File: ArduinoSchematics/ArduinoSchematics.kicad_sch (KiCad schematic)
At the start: 15 parts

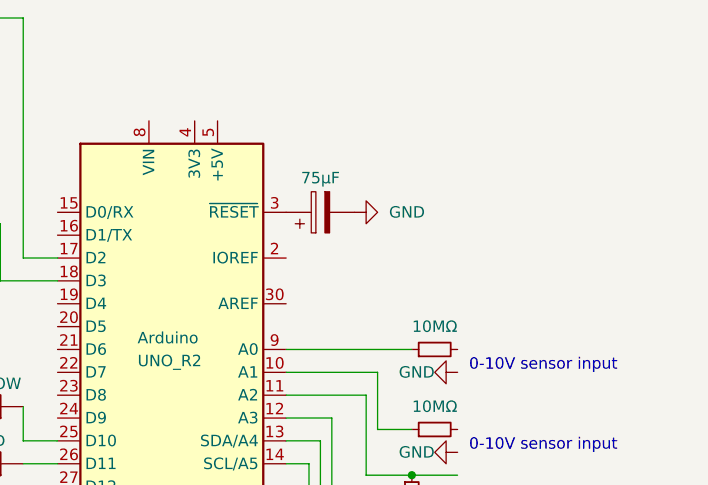
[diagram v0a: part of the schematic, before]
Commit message: Added switch to schematics
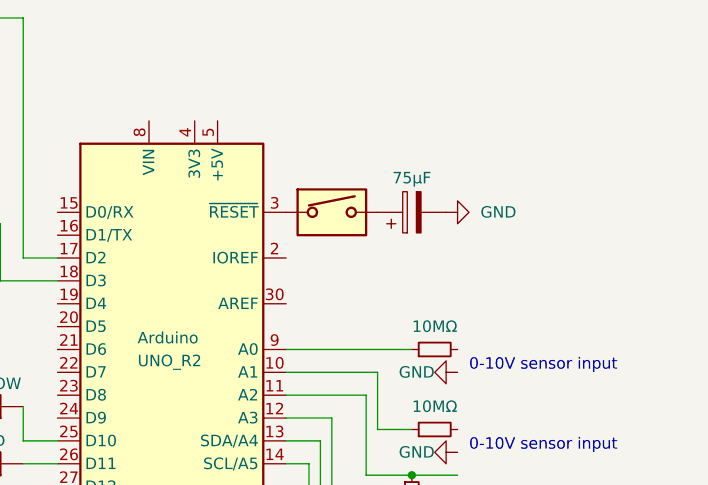
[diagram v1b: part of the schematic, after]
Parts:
- added U?: DG308AxY, Package_SO:SOIC-16_3.9x9.9mm_P1.27mm, symbol Analog_Switch:DG308AxY
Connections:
- net at Capacitor.1: no longer Arduino.3 (~{RESET})
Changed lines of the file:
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@@
     (pin "2")
   )
-  (symbol (lib_id "Device:C_Polarized") (at 138.43 68.58 90) (unit 1)
-    (in_bom yes) (on_board yes)
-    (property "Reference" "Capacitor" (id 0) (at 137.541 60.96 90)
-      (effects (font (size 1.27 1.27)) hide)
-    )
-    (property "Value" "75μF" (id 1) (at 138.43 64.77 90))
-    (property "Footprint" "test" (id 2) (at 142.24 67.6148 0)
-      (effects (font (size 1.27 1.27)) hide)
-    )
-    (property "Datasheet" "~" (id 3) (at 138.43 68.58 0)
+  (symbol (lib_id "Device:C_Polarized") (at 148.59 68.58 90) (unit 1)
+    (in_bom yes) (on_board yes)
+    (property "Reference" "Capacitor" (id 0) (at 147.701 60.96 90)
+      (effects (font (size 1.27 1.27)) hide)
+    )
+    (property "Value" "75μF" (id 1) (at 148.59 64.77 90))
+    (property "Footprint" "test" (id 2) (at 152.4 67.6148 0)
+      (effects (font (size 1.27 1.27)) hide)
+    )
+    (property "Datasheet" "~" (id 3) (at 148.59 68.58 0)
       (effects (font (size 1.27 1.27)) hide)
     )
@@
     (pin "2")
   )
-  (symbol (lib_id "power:GND") (at 142.24 68.58 90) (unit 1)
-    (in_bom yes) (on_board yes) (fields_autoplaced)
-    (property "Reference" "#PWR?" (id 0) (at 148.59 68.58 0)
-      (effects (font (size 1.27 1.27)) hide)
-    )
-    (property "Value" "GND" (id 1) (at 146.05 68.5799 90)
+  (symbol (lib_id "power:GND") (at 152.4 68.58 90) (unit 1)
+    (in_bom yes) (on_board yes) (fields_autoplaced)
+    (property "Reference" "#PWR?" (id 0) (at 158.75 68.58 0)
+      (effects (font (size 1.27 1.27)) hide)
+    )
+    (property "Value" "GND" (id 1) (at 156.21 68.5799 90)
       (effects (font (size 1.27 1.27)) (justify right))
     )
-    (property "Footprint" "" (id 2) (at 142.24 68.58 0)
-      (effects (font (size 1.27 1.27)) hide)
-    )
-    (property "Datasheet" "" (id 3) (at 142.24 68.58 0)
+    (property "Footprint" "" (id 2) (at 152.4 68.58 0)
+      (effects (font (size 1.27 1.27)) hide)
+    )
+    (property "Datasheet" "" (id 3) (at 152.4 68.58 0)
       (effects (font (size 1.27 1.27)) hide)
     )
@@
     )
     (pin "1")
+  )
+  (symbol (lib_id "Analog_Switch:DG308AxY") (at 139.7 68.58 0) (unit 1)
+    (in_bom yes) (on_board yes) (fields_autoplaced)
+    (property "Reference" "U?" (id 0) (at 139.7 63.5 0)
+      (effects (font (size 1.27 1.27)) hide)
+    )
+    (property "Value" "DG308AxY" (id 1) (at 139.7 63.5 0)
+      (effects (font (size 1.27 1.27)) hide)
+    )
+    (property "Footprint" "Package_SO:SOIC-16_3.9x9.9mm_P1.27mm" (id 2) (at 139.7 71.12 0)
+      (effects (font (size 1.27 1.27)) hide)
+    )
+    (property "Datasheet" "http://pdf.datasheetcatalog.com/datasheets/70/494502_DS.pdf" (id 3) (at 139.7 68.58 0)
+      (effects (font (size 1.27 1.27)) hide)
+    )
   )
   (symbol (lib_id "power:GND") (at 96.52 118.11 0) (unit 1)
@@
       (reference "RED") (unit 1) (value "LED") (footprint "")
     )
+    (path "/d7fdd219-dfe5-47bf-940c-6dc5e6afe90e"
+      (reference "U?") (unit 1) (value "DG308AxY") (footprint "Package_SO:SOIC-16_3.9x9.9mm_P1.27mm")
+    )
     (path "/1c04229f-a11d-4534-aa71-256db2af1807"

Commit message: New schematics
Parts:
- removed BLUE: LED, symbol Device:LED
- removed K?: DIPxx-1Axx-11x, Relay_THT:Relay_StandexMeder_DIP_LowProfile, symbol Relay:DIPxx-1Axx-11x
- removed R?: 250Ω, symbol Device:R_Small
- added GREEN: LED, symbol Device:LED
- added J?: Connection to analog sensor, symbol Connector:Screw_Terminal_01x06
- added J?: Common negative ground, symbol Connector:Screw_Terminal_01x03
- added J?: 0-5 V input/output to actuator, symbol Connector:Screw_Terminal_01x04
- added J?: 24V power line, symbol Connector:Screw_Terminal_01x02
- added R? (x4): 200Ω, symbol Device:R_Small
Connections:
- net GND: now also GREEN.1 (K), RED.1 (K), YELLOW.1 (K), GREEN.1 (K)
- net at K?.1, K?.14: now also J?.2 (Pin_2)
- net at Arduino.17 (D2), K?.2: now also R?.1
- net at K?.7, K?.8: now also J?.1 (Pin_1)
- net at YELLOW.2 (A): now also R?.1; no longer Arduino.25 (D10)
- net at GREEN.2 (A): now also R?.1; no longer Arduino.27 (D12)
- net at R?.2: now also J?.1 (Pin_1)
- net at Arduino.14 (SCL/A5), R?.1: now also J?.6 (Pin_6)
- net at Arduino.28 (D13): now also R?.2
- net at RED.2 (A): now also R?.1; no longer Arduino.26 (D11)
- net at Arduino.12 (A3), R?.1: now also J?.4 (Pin_4)
- net at R?.2: now also J?.2 (Pin_2)
- net at Arduino.13 (SDA/A4), R?.1: now also J?.5 (Pin_5)
- net at Arduino.18 (D3): now also J?.4 (Pin_4)
- net at Arduino.11 (A2), R?.1: now also J?.3 (Pin_3)
- net at Arduino.19 (D4): now also J?.3 (Pin_3)
- net at Arduino.20 (D5): now also J?.2 (Pin_2)
- net at Arduino.21 (D6): now also J?.1 (Pin_1)
- net at Arduino.29 (GND): now also J?.3 (Pin_3)
- net at Arduino.6 (GND): now also J?.2 (Pin_2)
- net at Arduino.7 (GND): now also J?.1 (Pin_1)
- new net: Arduino.27 (D12), R?.2
- new net: GREEN.2 (A), R?.2
- new net: Arduino.26 (D11), R?.2
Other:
- note added: "Filling valve power supply breakout"
- note removed: "Filling valve control"
- moved on the sheet: GREEN, RED, YELLOW

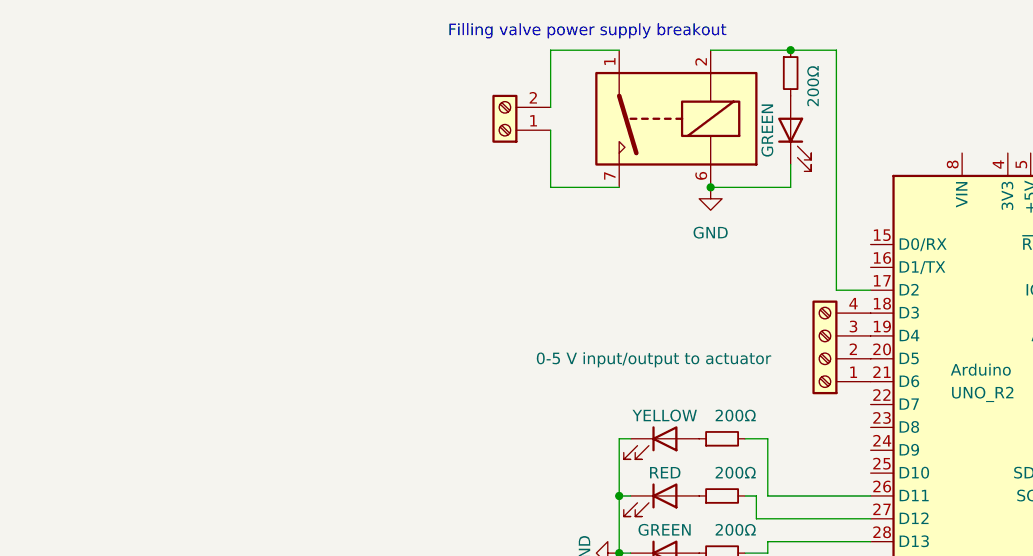
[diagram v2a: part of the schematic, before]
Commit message: added AC power supply, converter and actuator to schematic
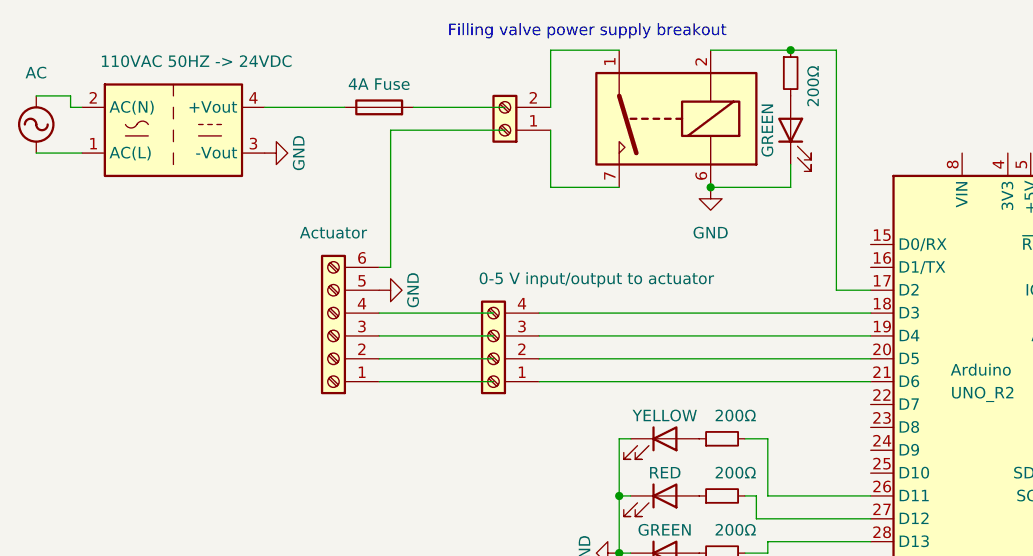
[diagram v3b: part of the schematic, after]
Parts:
- added F?: 4A Fuse, symbol Device:Fuse
- added J?: Actuator, symbol Connector:Screw_Terminal_01x06
- added PS?: 110VAC 50HZ -> 24VDC, Converter_ACDC:Converter_ACDC_RECOM_RAC01-xxSGB_THT, symbol Converter_ACDC:RAC01-3.3SGB
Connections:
- net GND: now also J?.5 (Pin_5), PS?.3 (-Vout)
- new net: F?.1, PS?.4 (+Vout)
- new net AC: PS?.1 (AC(L))
